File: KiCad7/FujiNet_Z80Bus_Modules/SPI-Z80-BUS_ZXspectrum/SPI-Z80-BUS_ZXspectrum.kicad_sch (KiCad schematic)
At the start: 31 parts, among them J2 PinHeader_2.54mm, J3 PinHeader_2.54mm, J4 PinHeader_2.54mm, J5 PinHeader_2.54mm, J6 PinHeader_2.54mm, J7 PinHeader_2.54mm

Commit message: Reorganised the project again
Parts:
- renumbered J3 to J?, J4 to J?, J7 to J?, J6 to J?, J5 to J?, J2 to J?

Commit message: KiCad ZXspectrum concept
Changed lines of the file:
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@@
     (comment 2 "SPI Bus to couple the ESP32 to the Local Bus and Z80 Bus")
   )
-  (bus_alias "ESP_SPI_INTERNAL" (members "ESP_SPI_INT.MOSI" "ESP_SPI_INT.SCK" "ESP_SPI_INT.MR" "ESP_SPI_INT.STC" "ESP_SPI_INT.CE" "ESP_SPI_INT.PL" "ESP_SPI_INT.MISO" "ESP_SPI_INT.OE" ""))
+  (bus_alias "SPI_INTERNAL" (members "ESP_SPI_INT.MOSI" "ESP_SPI_INT.SCK" "ESP_SPI_INT.MR" "ESP_SPI_INT.STC" "ESP_SPI_INT.CE" "ESP_SPI_INT.PL" "ESP_SPI_INT.MISO" "ESP_SPI_INT.OE" ""))
   (bus_alias "ESP_CONTROL" (members "ESP_CONTROL.RD" "ESP_CONTROL.WR" "ESP_CONTROL.IORQ" "ESP_CONTROL.MEMRQ" "ESP_CONTROL.BUSRQ" "ESP_CONTROL.WAIT" "ESP_CONTROL.ROMCS" "ESP_CONTROL.NMI"))
   (junction (at 168.91 128.27) (diameter 0) (color 0 0 0 0)
@@
     (effects (font (size 1.27 1.27)) (justify right))
   )
-  (hierarchical_label "{ESP_SPI_INTERNAL}" (shape input) (at 100.33 191.77 90) (fields_autoplaced)
+  (hierarchical_label "{SPI_INTERNAL}" (shape input) (at 100.33 191.77 90) (fields_autoplaced)
     (effects (font (size 1.27 1.27)) (justify left))
   )
@@
         )
         (path "/532c0392-800e-45cc-8170-6d32f2390e83/114594a1-f6a8-44ff-8b97-ba4e59160a11"
-          (reference "IC4") (unit 1)
+          (reference "Local_data.out1") (unit 1)
         )
       )
@@
   (symbol (lib_id "74xx:74HC595") (at 212.09 134.62 90) (unit 1)
     (in_bom yes) (on_board yes) (dnp no)
-    (property "Reference" "IC?" (at 215.9 133.35 90)
+    (property "Reference" "IC?" (at 213.36 133.35 90)
       (effects (font (size 1.4986 1.4986)))
     )
@@
         )
         (path "/532c0392-800e-45cc-8170-6d32f2390e83/114594a1-f6a8-44ff-8b97-ba4e59160a11"
-          (reference "IC9") (unit 1)
+          (reference "Local_addr_l.out1") (unit 1)
         )
       )
@@
   (symbol (lib_id "74xx:74HC595") (at 252.73 134.62 90) (unit 1)
     (in_bom yes) (on_board yes) (dnp no)
-    (property "Reference" "IC?" (at 255.27 133.35 90)
+    (property "Reference" "IC?" (at 254 133.35 90)
       (effects (font (size 1.4986 1.4986)))
     )
@@
         )
         (path "/532c0392-800e-45cc-8170-6d32f2390e83/114594a1-f6a8-44ff-8b97-ba4e59160a11"
-          (reference "IC10") (unit 1)
+          (reference "Local_addr_h.out1") (unit 1)
         )
       )
@@
         )
         (path "/532c0392-800e-45cc-8170-6d32f2390e83/114594a1-f6a8-44ff-8b97-ba4e59160a11"
-          (reference "IC1") (unit 1)
+          (reference "Local_data.in1") (unit 1)
         )
       )
@@
         )
         (path "/532c0392-800e-45cc-8170-6d32f2390e83/114594a1-f6a8-44ff-8b97-ba4e59160a11"
-          (reference "IC3") (unit 1)
+          (reference "Z80_control.in1") (unit 1)
         )
       )
@@
         )
         (path "/532c0392-800e-45cc-8170-6d32f2390e83/114594a1-f6a8-44ff-8b97-ba4e59160a11"
-          (reference "IC5") (unit 1)
+          (reference "Local_addr-l.in1") (unit 1)
         )
       )
@@
         )
         (path "/532c0392-800e-45cc-8170-6d32f2390e83/114594a1-f6a8-44ff-8b97-ba4e59160a11"
-          (reference "IC8") (unit 1)
+          (reference "Local_addr-h.in1") (unit 1)
         )
       )
@@
         )
         (path "/532c0392-800e-45cc-8170-6d32f2390e83/114594a1-f6a8-44ff-8b97-ba4e59160a11"
-          (reference "IC6") (unit 1)
+          (reference "ESP_Control1") (unit 1)
         )
       )
@@
   (symbol (lib_id "74xx:74HC244") (at 58.42 144.78 270) (unit 1)
     (in_bom yes) (on_board yes) (dnp no)
-    (property "Reference" "IC?" (at 64.77 147.32 90)
+    (property "Reference" "IC?" (at 58.42 146.05 90)
       (effects (font (size 1.4986 1.4986)))
     )
@@
         )
         (path "/532c0392-800e-45cc-8170-6d32f2390e83/114594a1-f6a8-44ff-8b97-ba4e59160a11"
-          (reference "IC2") (unit 1)
+          (reference "Control_selection1") (unit 1)
         )
       )
@@
         )
         (path "/532c0392-800e-45cc-8170-6d32f2390e83/114594a1-f6a8-44ff-8b97-ba4e59160a11"
-          (reference "IC7") (unit 1)
+          (reference "IC1") (unit 1)
         )
       )
@@
         )
         (path "/532c0392-800e-45cc-8170-6d32f2390e83/114594a1-f6a8-44ff-8b97-ba4e59160a11"
-          (reference "IC7") (unit 2)
+          (reference "IC1") (unit 2)
         )
       )
@@
         )
         (path "/532c0392-800e-45cc-8170-6d32f2390e83/114594a1-f6a8-44ff-8b97-ba4e59160a11"
-          (reference "IC7") (unit 4)
+          (reference "IC1") (unit 4)
         )
       )
@@
         )
         (path "/532c0392-800e-45cc-8170-6d32f2390e83/114594a1-f6a8-44ff-8b97-ba4e59160a11"
-          (reference "IC7") (unit 3)
+          (reference "IC1") (unit 3)
         )
       )
@@
         )
         (path "/532c0392-800e-45cc-8170-6d32f2390e83/114594a1-f6a8-44ff-8b97-ba4e59160a11"
-          (reference "IC7") (unit 5)
+          (reference "IC1") (unit 5)
         )
       )

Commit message: KiCad Cleaned up SPI schem
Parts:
- removed D? (x2): 1N4148, Diode_THT:D_T-1_P5.08mm_Horizontal, symbol Device:D
- removed IC? (x4): 74595N, Package_DIP:DIP-16_W7.62mm_Socket, symbol 74xx:74HC595
- removed IC? (x4): 74HC165N, Package_DIP:DIP-16_W7.62mm_Socket, symbol 74xx:74HC165
- removed IC? (x4): 74HC32N, Package_DIP:DIP-14_W7.62mm_Socket, symbol 74xx:74LS32
- removed RN? (x2): 4609M-101-103LF, Resistor_THT:R_Array_SIP9, symbol Device:R_Network08
- added D3, D4: 1N4148, Diode_THT:D_T-1_P5.08mm_Horizontal, symbol Device:D
- added ESP_CONTROL.Bias, LOCAL_D.Bias: 4609M-101-103LF, Resistor_THT:R_Array_SIP9, symbol Device:R_Network08
- RN?: value LOCAL_CONTROL_BIAS -> LOCAL_CONTROL.Bias
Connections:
- net +5V: now also R?.2, D3.2 (A), D4.2 (A); no longer R?.1
- net ESP_CONTROL.BUSRQ: now also ESP_CONTROL.Bias.6 (R5)
- net ESP_CONTROL.IORQ: now also ESP_CONTROL.Bias.4 (R3)
- net ESP_CONTROL.MEMRQ: now also ESP_CONTROL.Bias.5 (R4)
- net ESP_CONTROL.NMI: now also ESP_CONTROL.Bias.9 (R8)
- net ESP_CONTROL.RD: now also ESP_CONTROL.Bias.2 (R1)
- net ESP_CONTROL.ROMCS: now also ESP_CONTROL.Bias.8 (R7)
- net ESP_CONTROL.WAIT: now also ESP_CONTROL.Bias.7 (R6)
- net ESP_CONTROL.WR: now also ESP_CONTROL.Bias.3 (R2)
- net ESP_SPI_INT.MR: now also R?.1; no longer J?.3 (Pin_3), R?.2
- net LOCAL_D0: now also LOCAL_D.Bias.2 (R1)
- net LOCAL_D1: now also LOCAL_D.Bias.3 (R2)
- net LOCAL_D2: now also LOCAL_D.Bias.4 (R3)
- net LOCAL_D3: now also LOCAL_D.Bias.5 (R4)
- net LOCAL_D4: now also LOCAL_D.Bias.6 (R5)
- net LOCAL_D5: now also LOCAL_D.Bias.7 (R6)
- net LOCAL_D6: now also LOCAL_D.Bias.8 (R7)
- net LOCAL_D7: now also LOCAL_D.Bias.9 (R8)
- net ESP_CONTROL.WR+ESP_PULSE: no longer names the net of IC?.11, IC?.15 (2A1), IC?.4 (1A1)
- new net: D4.1 (K), ESP_CONTROL.Bias.1 (common)
- new net: D3.1 (K), LOCAL_D.Bias.1 (common)
- new net ESP_SPI_INT.STC: J?.3 (Pin_3)
- no-connect marks 12 -> 4
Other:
- added sheet SPI-Z080-BUS_read (SPI-Z080-BUS_read.kicad_sch)
- added sheet SPI-Z080-BUS_write (SPI-Z080-BUS_write.kicad_sch)
- moved on the sheet: D12, D13, D14, D15, D?, IC?, IC?D, J?, R?, RN?

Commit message: KiCad - SPI bus impl
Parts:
- removed J? (x6): PinHeader_2.54mm, Connector_PinHeader_2.54mm:PinHeader_1x08_P2.54mm_Vertical, symbol Connector:Conn_01x08_Socket
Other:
- sheet SPI-Z080-BUS_read renamed SPI-Z80-BUS_read
- sheet SPI-Z080-BUS_write renamed SPI-Z80-BUS_write
- sheet SPI-Z80-BUS_read: file SPI-Z080-BUS_read.kicad_sch -> SPI-Z80-BUS_read.kicad_sch
- sheet SPI-Z80-BUS_write: file SPI-Z080-BUS_write.kicad_sch -> SPI-Z80-BUS_write.kicad_sch
- moved on the sheet: ESP_CONTROL.Bias

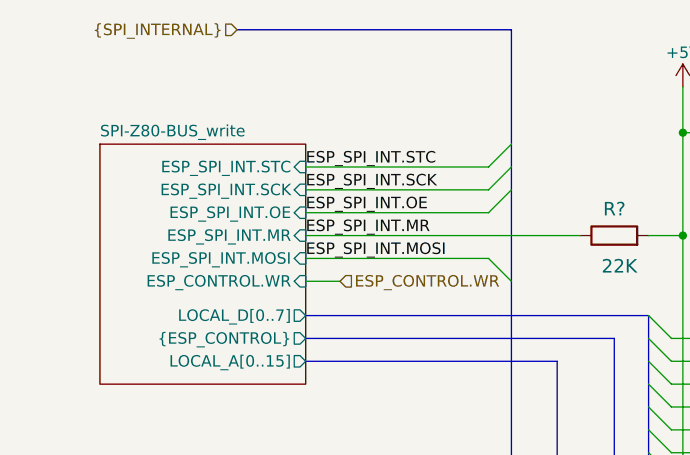
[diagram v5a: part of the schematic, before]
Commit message: KICad fixed SPI impl
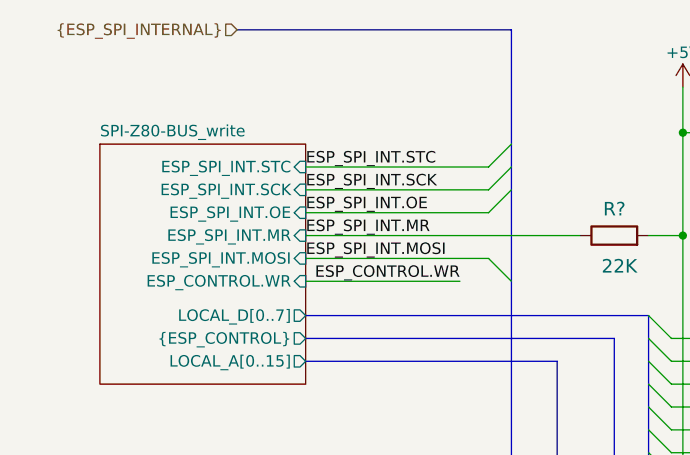
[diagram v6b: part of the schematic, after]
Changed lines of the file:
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@@
     (comment 2 "SPI Bus to couple the ESP32 to the Local Bus and Z80 Bus")
   )
+  (bus_alias "ESP_SPI_INTERNAL" (members "ESP_SPI_INT.MOSI" "ESP_SPI_INT.SCK" "ESP_SPI_INT.MR" "ESP_SPI_INT.STC" "ESP_SPI_INT.CE" "ESP_SPI_INT.PL" "ESP_SPI_INT.MISO" "ESP_SPI_INT.OE" ""))
   (bus_alias "LOCAL_CONTROL" (members "LOCAL_CONTROL.RD" "LOCAL_CONTROL.WR" "LOCAL_CONTROL.IORQ" "LOCAL_CONTROL.MEMRQ"))
   (bus_alias "ESP_CONTROL" (members "ESP_CONTROL.RD" "ESP_CONTROL.WR" "ESP_CONTROL.IORQ" "ESP_CONTROL.MEMRQ" "ESP_CONTROL.BUSRQ" "ESP_CONTROL.WAIT" "ESP_CONTROL.ROMCS" "ESP_CONTROL.NMI"))
-  (bus_alias "SPI_INTERNAL" (members "ESP_SPI_INT.MOSI" "ESP_SPI_INT.SCK" "ESP_SPI_INT.MR" "ESP_SPI_INT.STC" "ESP_SPI_INT.CE" "ESP_SPI_INT.PL" "ESP_SPI_INT.MISO" "ESP_SPI_INT.OE" ""))
   (junction (at 99.06 55.88) (diameter 0) (color 0 0 0 0)
   )
@@
     (stroke (width 0) (type default))
   )
-  (wire (pts (xy 45.72 49.53) (xy 41.91 49.53))
+  (wire (pts (xy 59.055 49.53) (xy 41.91 49.53))
     (stroke (width 0) (type default))
   )
@@
     (effects (font (size 1.27 1.27)) (justify left bottom))
   )
+  (label "ESP_CONTROL.WR" (at 59.055 49.53 180) (fields_autoplaced)
+    (effects (font (size 1.27 1.27)) (justify right bottom))
+  )
   (label "ESP_CONTROL.NMI" (at 147.32 120.65 0) (fields_autoplaced)
     (effects (font (size 1.27 1.27)) (justify left bottom))
@@
     (effects (font (size 1.27 1.27)) (justify left bottom))
   )
-  (hierarchical_label "{SPI_INTERNAL}" (shape input) (at 34.29 21.59 180) (fields_autoplaced)
+  (hierarchical_label "{ESP_SPI_INTERNAL}" (shape input) (at 34.29 21.59 180) (fields_autoplaced)
     (effects (font (size 1.27 1.27)) (justify right))
   )
   (hierarchical_label "{ESP_CONTROL}" (shape output) (at 76.2 163.83 270) (fields_autoplaced)
     (effects (font (size 1.27 1.27)) (justify right))
-  )
-  (hierarchical_label "ESP_CONTROL.WR" (shape input) (at 45.72 49.53 0) (fields_autoplaced)
-    (effects (font (size 1.27 1.27)) (justify left))
   )
   (hierarchical_label "LOCAL_A[0..15]" (shape bidirectional) (at 69.85 163.83 270) (fields_autoplaced)
@@
       (project "SPI-Z80-BUS_ZXspectrum_impl"
         (path "/532c0392-800e-45cc-8170-6d32f2390e83/9a993edb-7f20-4cca-a657-2a2140304b51"
-          (reference "#PWR01") (unit 1)
+          (reference "#PWR03") (unit 1)
         )
       )
@@
       (project "SPI-Z80-BUS_ZXspectrum_impl"
         (path "/532c0392-800e-45cc-8170-6d32f2390e83/9a993edb-7f20-4cca-a657-2a2140304b51"
-          (reference "#PWR02") (unit 1)
-        )
-      )
+          (reference "#PWR04") (unit 1)
+        )
+      )
